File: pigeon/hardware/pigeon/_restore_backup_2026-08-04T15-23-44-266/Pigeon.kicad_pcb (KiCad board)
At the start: 2 copper layers, 120 x 30 mm, 16 parts, among them J1 Battery, SW1 Power Switch, U1 ESP32-S3-Zero, U2 Adafruit_Ultimate_GPS, U3 Adafruit_RFM95W

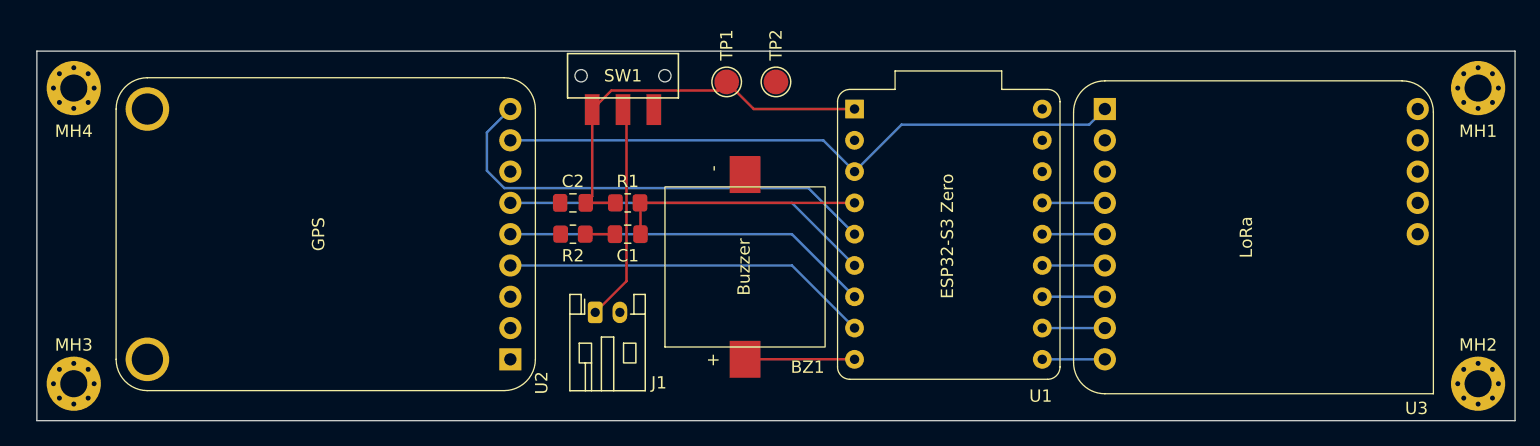
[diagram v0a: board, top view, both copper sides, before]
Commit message: pigeon: pcb layout mostly completed. Layed everything out and added mounting holes
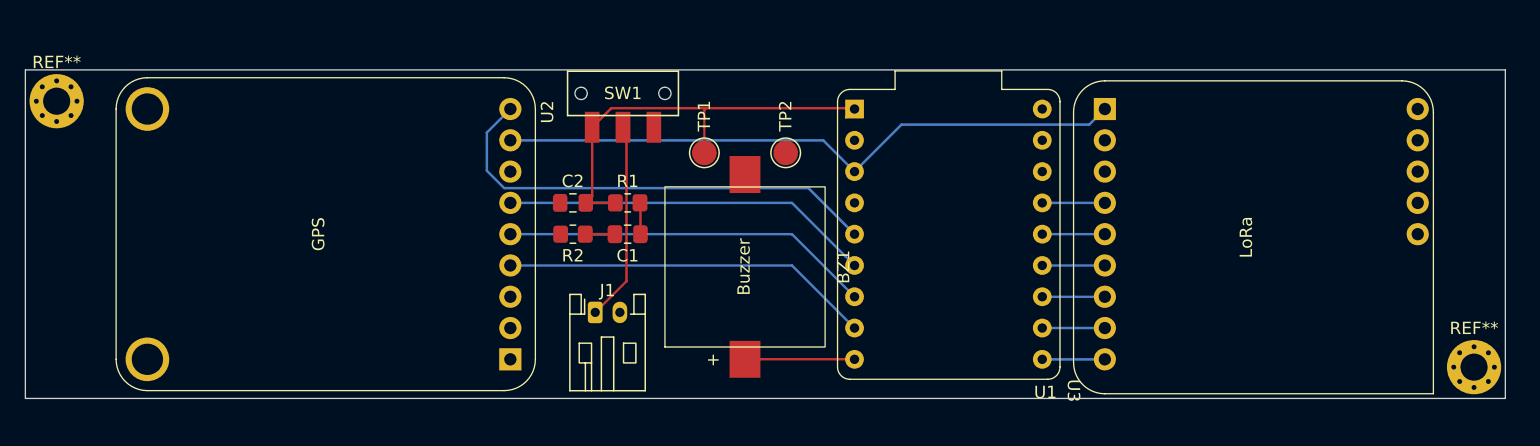
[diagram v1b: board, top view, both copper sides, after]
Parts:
- removed MH1, MH2, MH3, MH4: MountingHole_Pad, MountingHole:MountingHole_2.2mm_M2_Pad_Via
- added REF**: MountingHole_2.2mm_M2_Pad_Via, MountingHole:MountingHole_2.2mm_M2_Pad_Via, F.Cu at (169.7, 97.2)
- added REF**: MountingHole_2.2mm_M2_Pad_Via, MountingHole:MountingHole_2.2mm_M2_Pad_Via, F.Cu at (54.6, 75.6)
- moved TP1 6.03 mm to (107.2, 79.8)
- moved TP2 5.81 mm to (113.8, 79.8)
- moved SW1 1.43 mm to (100.6, 74.9)
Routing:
- net /VBAT_SENSE: track 20.0 -> 2.56 mm
- net /VBAT: track 33.3 -> 35.4 mm
- net Net-(J1-Pin_1): track 17.6 -> 16.2 mm
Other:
- board size 120 x 30 mm -> 120.1 x 26.7 mm
